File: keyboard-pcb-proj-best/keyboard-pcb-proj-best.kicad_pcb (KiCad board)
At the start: 2 copper layers, 86 x 38.5 mm, 24 parts, among them SW1 SW_PUSH, U1 ATmega32U4-A, Y1 16Mhz

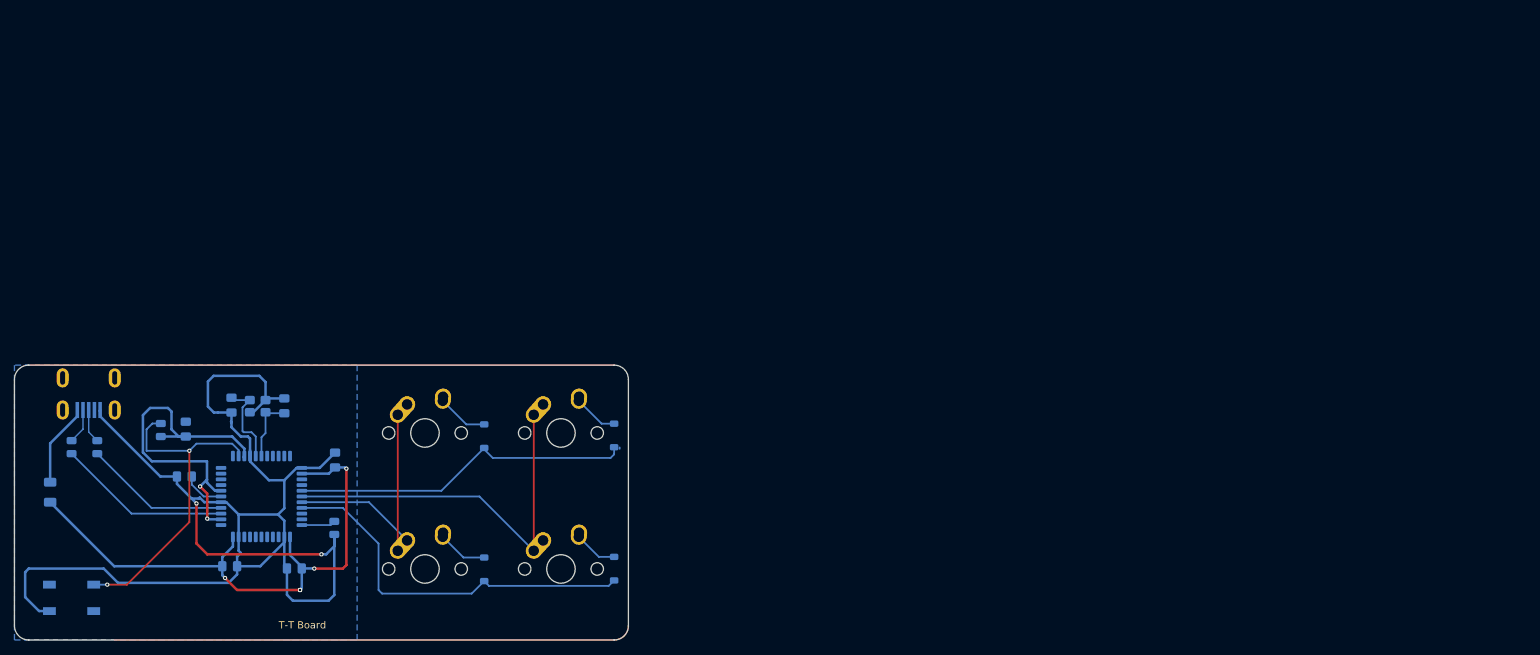
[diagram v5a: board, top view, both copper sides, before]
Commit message: PCB design rework started
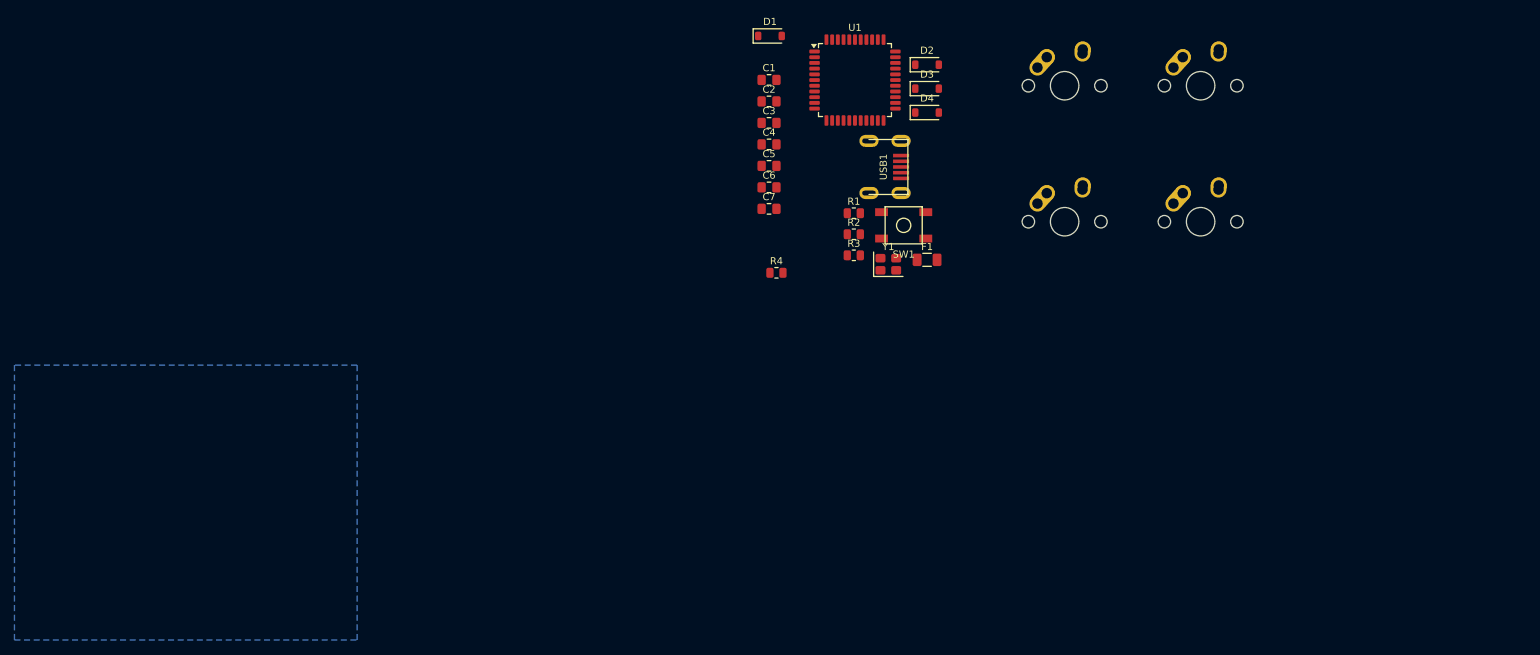
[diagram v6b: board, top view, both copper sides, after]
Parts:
- C1, C2, C3, C4, C5, C6, C7, D1, D2, D3, D4, F1, R1, R2, R3, R4, SW1, U1, USB1, Y1: moved to F.Cu
- moved SW1 127.7 mm to (192.6, 62.4), turned to 0 degrees
- moved F1 127.1 mm to (195.8, 67.2), turned to 0 degrees
- moved MX1 119.0 mm to (234.2, 42.9)
- moved USB1 113.2 mm to (187.7, 54.2), turned to 0 degrees
- moved R3 112.8 mm to (185.6, 66.6), turned to 0 degrees
- moved R2 110.1 mm to (185.6, 63.7), turned to 0 degrees
- moved MX3 102.0 mm to (215.1, 61.9)
- moved MX4 102.0 mm to (234.2, 61.9)
- moved U1 101.6 mm to (185.7, 42.1)
- moved C1 99.0 mm to (173.7, 42.0), turned to 0 degrees
- moved C5 94.1 mm to (173.7, 54.1)
- moved C2 93.3 mm to (173.7, 45.1), turned to 0 degrees
- moved D3 91.6 mm to (195.8, 43.3), turned to 0 degrees
- moved C4 90.9 mm to (173.7, 51.1), turned to 0 degrees
- moved Y1 90.5 mm to (190.4, 67.9), turned to 0 degrees
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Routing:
- net GND: track 198.7 -> 0.00 mm, vias 2 -> 0
- net +5V: track 132.0 -> 0.00 mm, vias 7 -> 0
- net COL1: track 54.7 -> 0.00 mm
- net ROW1: track 53.8 -> 0.00 mm
- net ROW0: track 48.3 -> 0.00 mm
- net Net-(U1-~{RESET}): track 47.5 -> 0.00 mm, vias 2 -> 0
- net COL0: track 36.0 -> 0.00 mm
- net Net-(U1-D-): track 24.4 -> 0.00 mm
- net Net-(U1-D+): track 20.5 -> 0.00 mm
- net Net-(U1-XTAL2): track 12.4 -> 0.00 mm
- net VCC: track 11.7 -> 0.00 mm
- net Net-(U1-XTAL1): track 9.33 -> 0.00 mm
- net Net-(D1-A): track 7.17 -> 0.00 mm
- net Net-(D3-A): track 7.00 -> 0.00 mm
- net Net-(D4-A): track 6.71 -> 0.00 mm
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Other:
- board outline removed
- board text removed: "T-T Board"

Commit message: Update keyboard-pcb-proj-best.kicad_pcb
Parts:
- moved D1 93.0 mm to (255.6, 80.2)
- moved USB1 87.3 mm to (273.8, 68.3)
- moved D2 67.2 mm to (262.8, 45.9)
- moved D3 67.2 mm to (262.8, 49.2)
- moved D4 67.2 mm to (262.8, 52.6)
- moved C1 67.0 mm to (230.9, 77.0)
- moved C2 67.0 mm to (230.9, 80.0)
- moved C3 67.0 mm to (230.9, 83.0)
- moved C4 67.0 mm to (230.9, 86.0)
- moved C5 67.0 mm to (230.9, 89.0)
- moved C6 67.0 mm to (230.9, 92.0)
- moved C7 67.0 mm to (230.9, 95.0)
- moved R4 67.0 mm to (231.9, 104.0)
- moved U1 26.4 mm to (188.9, 68.3)
- moved R1 23.7 mm to (201.1, 78.6)
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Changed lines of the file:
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@@
 	(footprint "Capacitor_SMD:C_0805_2012Metric_Pad1.18x1.45mm_HandSolder"
 		(layer "F.Cu")
-		(at 173.7 45.05875)
+		(at 230.85625 79.97125)
 		(descr "Capacitor SMD 0805 (2012 Metric), square (rectangular) end terminal, IPC-7351 nominal with elongated pad for handsoldering. (Body size source: IPC-SM-782 page 76, https://www.pcb-3d.com/wordpress/wp-content/uploads/ipc-sm-782a_amendment_1_and_2.pdf, https://docs.google.com/spreadsheets/d/1BsfQQcO9C6DZCsRaXUlFlo91Tg2WpOkGARC1WS5S8t0/edit?usp=sharing), generated with kicad-footprint-generator")
 		(tags "capacitor handsolder")
@@
 	(footprint "MX_Alps_Hybrid:MX-1U-NoLED"
 		(layer "F.Cu")
-		(at 234.15625 42.8625)
+		(at 215.10625 42.8625)
 		(property "Reference" "MX1"
 			(at 0 3.175 0)
@@
 	(footprint "Resistor_SMD:R_0805_2012Metric"
 		(layer "F.Cu")
-		(at 174.7375 69.06875)
+		(at 231.89375 103.98125)
 		(descr "Resistor SMD 0805 (2012 Metric), square (rectangular) end terminal, IPC-7351 nominal, (Body size source: IPC-SM-782 page 72, https://www.pcb-3d.com/wordpress/wp-content/uploads/ipc-sm-782a_amendment_1_and_2.pdf), generated with kicad-footprint-generator")
 		(tags "resistor")
@@
 	(footprint "Capacitor_SMD:C_0805_2012Metric_Pad1.18x1.45mm_HandSolder"
 		(layer "F.Cu")
-		(at 173.7 48.06875)
+		(at 230.85625 82.98125)
 		(descr "Capacitor SMD 0805 (2012 Metric), square (rectangular) end terminal, IPC-7351 nominal with elongated pad for handsoldering. (Body size source: IPC-SM-782 page 76, https://www.pcb-3d.com/wordpress/wp-content/uploads/ipc-sm-782a_amendment_1_and_2.pdf, https://docs.google.com/spreadsheets/d/1BsfQQcO9C6DZCsRaXUlFlo91Tg2WpOkGARC1WS5S8t0/edit?usp=sharing), generated with kicad-footprint-generator")
 		(tags "capacitor handsolder")
@@
 	(footprint "Crystal:Crystal_SMD_3225-4Pin_3.2x2.5mm"
 		(layer "F.Cu")
-		(at 190.4075 67.86875)
+		(at 205.8875 85.78125)
 		(descr "SMD3225/4, Crystal, 3.2x2.5mm package, SMD, generated with kicad-footprint-generator make_crystal.py, http://www.txccrystal.com/images/pdf/7m-accuracy.pdf")
 		(property "Reference" "Y1"
@@
 	(footprint "Capacitor_SMD:C_0805_2012Metric_Pad1.18x1.45mm_HandSolder"
 		(layer "F.Cu")
-		(at 173.7 51.07875)
+		(at 230.85625 85.99125)
 		(descr "Capacitor SMD 0805 (2012 Metric), square (rectangular) end terminal, IPC-7351 nominal with elongated pad for handsoldering. (Body size source: IPC-SM-782 page 76, https://www.pcb-3d.com/wordpress/wp-content/uploads/ipc-sm-782a_amendment_1_and_2.pdf, https://docs.google.com/spreadsheets/d/1BsfQQcO9C6DZCsRaXUlFlo91Tg2WpOkGARC1WS5S8t0/edit?usp=sharing), generated with kicad-footprint-generator")
 		(tags "capacitor handsolder")
@@
 	(footprint "MX_Alps_Hybrid:MX-1U-NoLED"
 		(layer "F.Cu")
-		(at 215.10625 42.8625)
+		(at 234.15625 42.8625)
 		(property "Reference" "MX2"
 			(at 0 3.175 0)
@@
 	(footprint "Resistor_SMD:R_0805_2012Metric"
 		(layer "F.Cu")
-		(at 185.5775 66.61875)
+		(at 201.0575 84.53125)
 		(descr "Resistor SMD 0805 (2012 Metric), square (rectangular) end terminal, IPC-7351 nominal, (Body size source: IPC-SM-782 page 72, https://www.pcb-3d.com/wordpress/wp-content/uploads/ipc-sm-782a_amendment_1_and_2.pdf), generated with kicad-footprint-generator")
 		(tags "resistor")
@@
 	(footprint "Package_QFP:TQFP-44_10x10mm_P0.8mm"
 		(layer "F.Cu")
-		(at 185.7375 42.06875)
+		(at 188.9125 68.2625)
 		(descr "TQFP, 44 Pin (JEDEC MS-026 variation ACB, 1.00mm body thickness, https://www.jedec.org/document_search?search_api_views_fulltext=MS-026, https://ww1.microchip.com/downloads/en/PackagingSpec/00000049BZ.pdf#page=658), generated with kicad-footprint-generator ipc_gullwing_generator.py")
 		(tags "TQFP QFP Microchip_44-Lead-Plastic-Thin-Quad-Flatpack-(PT)")
@@
 	(footprint "Resistor_SMD:R_0805_2012Metric"
 		(layer "F.Cu")
-		(at 185.5775 63.66875)
+		(at 201.0575 81.58125)
 		(descr "Resistor SMD 0805 (2012 Metric), square (rectangular) end terminal, IPC-7351 nominal, (Body size source: IPC-SM-782 page 72, https://www.pcb-3d.com/wordpress/wp-content/uploads/ipc-sm-782a_amendment_1_and_2.pdf), generated with kicad-footprint-generator")
 		(tags "resistor")
@@
 	(footprint "random-keyboard-parts:Molex-0548190589"
 		(layer "F.Cu")
-		(at 187.6975 54.24375)
+		(at 273.84375 68.2625)
 		(property "Reference" "USB1"
 			(at 2.032 0 90)
@@
 	(footprint "Capacitor_SMD:C_0805_2012Metric_Pad1.18x1.45mm_HandSolder"
 		(layer "F.Cu")
-		(at 173.7 54.08875)
+		(at 230.85625 89.00125)
 		(descr "Capacitor SMD 0805 (2012 Metric), square (rectangular) end terminal, IPC-7351 nominal with elongated pad for handsoldering. (Body size source: IPC-SM-782 page 76, https://www.pcb-3d.com/wordpress/wp-content/uploads/ipc-sm-782a_amendment_1_and_2.pdf, https://docs.google.com/spreadsheets/d/1BsfQQcO9C6DZCsRaXUlFlo91Tg2WpOkGARC1WS5S8t0/edit?usp=sharing), generated with kicad-footprint-generator")
 		(tags "capacitor handsolder")
@@
 	(footprint "Capacitor_SMD:C_0805_2012Metric_Pad1.18x1.45mm_HandSolder"
 		(layer "F.Cu")
-		(at 173.7 57.09875)
+		(at 230.85625 92.01125)
 		(descr "Capacitor SMD 0805 (2012 Metric), square (rectangular) end terminal, IPC-7351 nominal with elongated pad for handsoldering. (Body size source: IPC-SM-782 page 76, https://www.pcb-3d.com/wordpress/wp-content/uploads/ipc-sm-782a_amendment_1_and_2.pdf, https://docs.google.com/spreadsheets/d/1BsfQQcO9C6DZCsRaXUlFlo91Tg2WpOkGARC1WS5S8t0/edit?usp=sharing), generated with kicad-footprint-generator")
 		(tags "capacitor handsolder")
@@
 	(footprint "Diode_SMD:D_SOD-123"
 		(layer "F.Cu")
-		(at 195.8325 39.91875)
+		(at 262.79375 45.8625)
 		(descr "SOD-123")
 		(tags "SOD-123")
@@
 	(footprint "Diode_SMD:D_SOD-123"
 		(layer "F.Cu")
-		(at 173.8325 35.88875)
+		(at 255.5875 80.16875)
 		(descr "SOD-123")
 		(tags "SOD-123")
@@
 	(footprint "Fuse:Fuse_1206_3216Metric"
 		(layer "F.Cu")
-		(at 195.8375 67.24875)
+		(at 211.3175 85.16125)
 		(descr "Fuse SMD 1206 (3216 Metric), square (rectangular) end terminal, IPC-7351 nominal, (Body size source: http://www.tortai-tech.com/upload/download/2011102023233369053.pdf), generated with kicad-footprint-generator")
 		(tags "fuse")
@@
 	(footprint "Diode_SMD:D_SOD-123"
 		(layer "F.Cu")
-		(at 195.8325 43.26875)
+		(at 262.79375 49.2125)
 		(descr "SOD-123")
 		(tags "SOD-123")
@@
 	(footprint "Resistor_SMD:R_0805_2012Metric"
 		(layer "F.Cu")
-		(at 185.5775 60.71875)
+		(at 201.0575 78.63125)
 		(descr "Resistor SMD 0805 (2012 Metric), square (rectangular) end terminal, IPC-7351 nominal, (Body size source: IPC-SM-782 page 72, https://www.pcb-3d.com/wordpress/wp-content/uploads/ipc-sm-782a_amendment_1_and_2.pdf), generated with kicad-footprint-generator")
 		(tags "resistor")
@@
 	(footprint "Capacitor_SMD:C_0805_2012Metric_Pad1.18x1.45mm_HandSolder"
 		(layer "F.Cu")
-		(at 173.7 60.10875)
+		(at 230.85625 95.02125)
 		(descr "Capacitor SMD 0805 (2012 Metric), square (rectangular) end terminal, IPC-7351 nominal with elongated pad for handsoldering. (Body size source: IPC-SM-782 page 76, https://www.pcb-3d.com/wordpress/wp-content/uploads/ipc-sm-782a_amendment_1_and_2.pdf, https://docs.google.com/spreadsheets/d/1BsfQQcO9C6DZCsRaXUlFlo91Tg2WpOkGARC1WS5S8t0/edit?usp=sharing), generated with kicad-footprint-generator")
 		(tags "capacitor handsolder")
@@
 	(footprint "Capacitor_SMD:C_0805_2012Metric_Pad1.18x1.45mm_HandSolder"
 		(layer "F.Cu")
-		(at 173.7 42.04875)
+		(at 230.85625 76.96125)
 		(descr "Capacitor SMD 0805 (2012 Metric), square (rectangular) end terminal, IPC-7351 nominal with elongated pad for handsoldering. (Body size source: IPC-SM-782 page 76, https://www.pcb-3d.com/wordpress/wp-content/uploads/ipc-sm-782a_amendment_1_and_2.pdf, https://docs.google.com/spreadsheets/d/1BsfQQcO9C6DZCsRaXUlFlo91Tg2WpOkGARC1WS5S8t0/edit?usp=sharing), generated with kicad-footprint-generator")
 		(tags "capacitor handsolder")
@@
 	(footprint "random-keyboard-parts:SKQG-1155865"
 		(layer "F.Cu")
-		(at 192.5575 62.41875)
+		(at 208.0375 80.33125)
 		(property "Reference" "SW1"
 			(at 0 4.064 0)
@@
 	(footprint "Diode_SMD:D_SOD-123"
 		(layer "F.Cu")
-		(at 195.8325 46.61875)
+		(at 262.79375 52.5625)
 		(descr "SOD-123")
 		(tags "SOD-123")

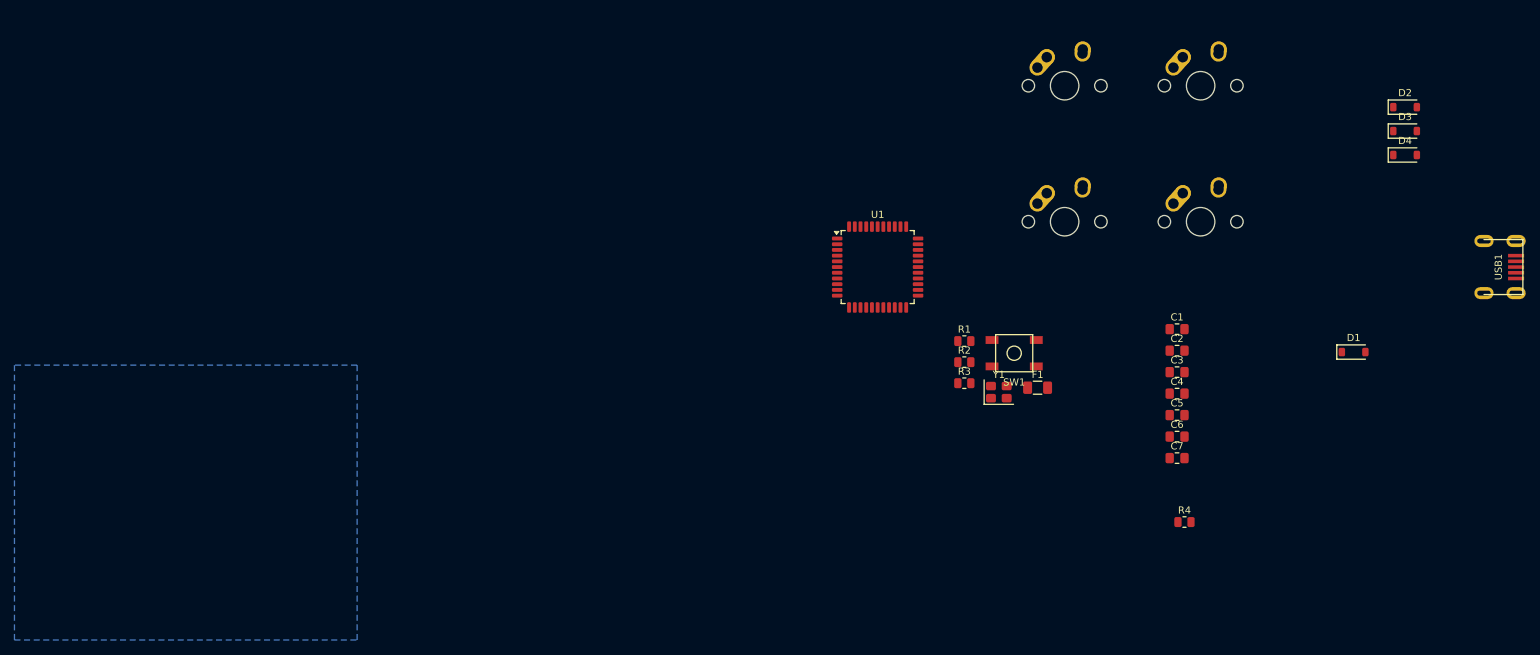
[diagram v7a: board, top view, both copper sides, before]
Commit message: Finished rerouting
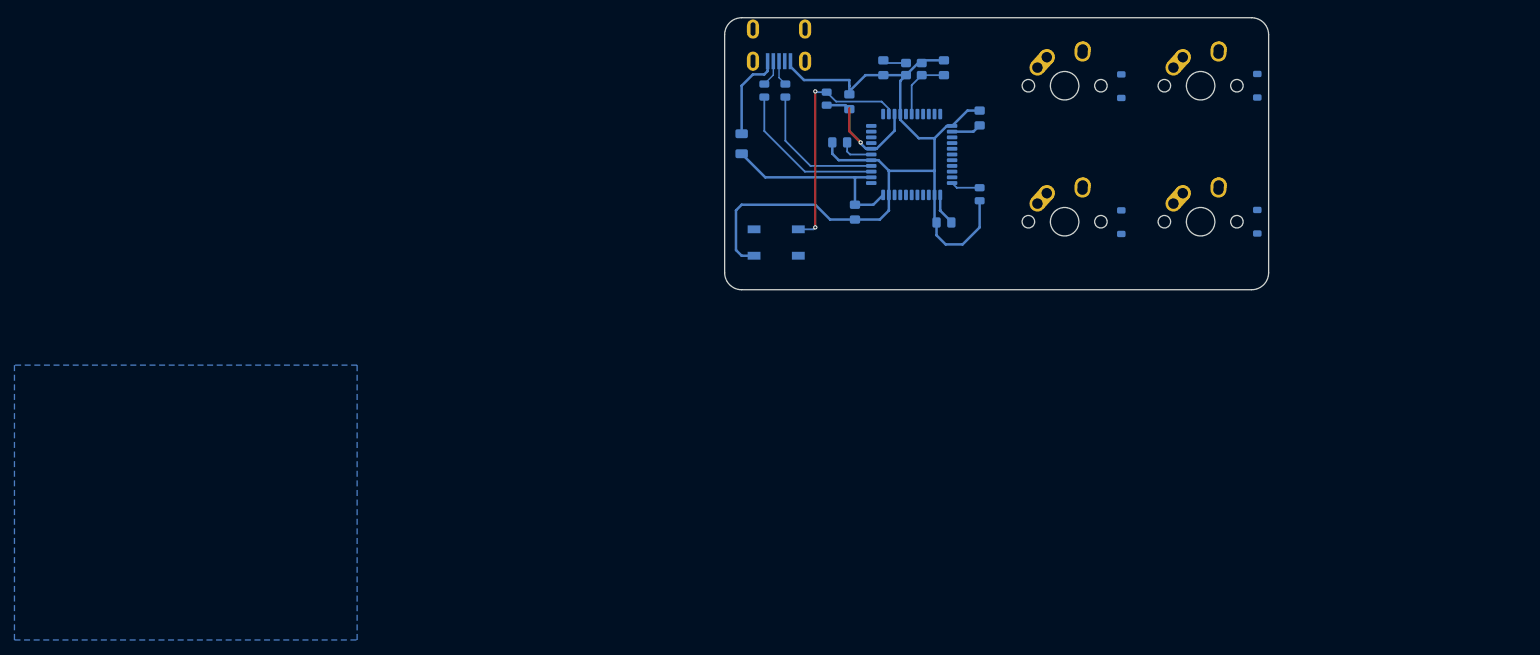
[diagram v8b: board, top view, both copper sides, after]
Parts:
- C1, C2, C3, C4, C5, C6, C7, D1, D2, D3, D4, F1, R1, R2, R3, R4, SW1, U1, USB1, Y1: moved to B.Cu
- moved USB1 104.2 mm to (175.1, 34.9), turned to -90 degrees
- moved R4 77.6 mm to (181.8, 44.7), turned to 90 degrees
- moved C7 68.4 mm to (189.7, 40.3), turned to 90 degrees
- moved C6 61.1 mm to (198.2, 40.3), turned to -90 degrees
- moved C2 57.6 mm to (184.9, 45.1), turned to 90 degrees
- moved C1 54.0 mm to (183.6, 50.8), turned to 180 degrees
- moved F1 53.7 mm to (169.9, 51.0), turned to 90 degrees
- moved C5 53.3 mm to (185.7, 60.6), turned to -90 degrees
- moved R3 49.7 mm to (173.0, 43.5), turned to 90 degrees
- moved D1 49.5 mm to (223.0, 42.9), turned to 90 degrees
- moved C4 47.5 mm to (203.2, 47.4), turned to 90 degrees
- moved Y1 46.8 mm to (194.0, 40.5), turned to 180 degrees
- moved R2 45.6 mm to (176.0, 43.5), turned to 90 degrees
- moved D3 41.7 mm to (223.0, 62.0), turned to 90 degrees
- moved C3 38.8 mm to (198.2, 62.0), turned to 180 degrees
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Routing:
- net GND: track 0.00 -> 126.7 mm
- net +5V: track 0.00 -> 54.0 mm, vias 0 -> 1
- net Net-(U1-~{RESET}): track 0.00 -> 33.6 mm, vias 0 -> 2
- net Net-(U1-D-): track 0.00 -> 22.1 mm
- net Net-(U1-D+): track 0.00 -> 19.6 mm
- net VCC: track 0.00 -> 12.6 mm
- net Net-(U1-XTAL1): track 0.00 -> 9.14 mm
- net Net-(U1-UCAP): track 0.00 -> 4.83 mm
- net Net-(U1-~{HWB}/PE2): track 0.00 -> 4.13 mm
- net D-: track 0.00 -> 3.72 mm
- net D+: track 0.00 -> 3.57 mm
- net Net-(U1-XTAL2): track 0.00 -> 3.33 mm
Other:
- board outline added: 76.2 x 38.1 mm
